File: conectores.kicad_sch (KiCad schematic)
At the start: 12 parts, among them J10 5v Input, J11 12v Input, J12 Temp DHT22, J2 Fan1 Conn, J3 Fan2 Conn, J4 Fan4 Conn, J5 Fan3 Conn, J6 Buzz Conn, J7 OLED, J8 Relay Ctrl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

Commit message: pop stashed changes
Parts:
- removed J10: 5v Input, Connector_PinHeader_2.54mm:PinHeader_1x02_P2.54mm_Vertical, symbol Connector:Conn_01x02_Male
- removed J11: 12v Input, Connector_PinHeader_2.54mm:PinHeader_1x02_P2.54mm_Vertical, symbol Connector:Conn_01x02_Male
- removed J6: Buzz Conn, Connector_PinHeader_2.54mm:PinHeader_1x03_P2.54mm_Vertical, symbol Connector:Conn_01x03_Male
- removed J8: Relay Ctrl, Connector_PinHeader_2.54mm:PinHeader_1x03_P2.54mm_Vertical, symbol Connector:Conn_01x03_Male
- removed J9: Relay Out, Connector_PinHeader_2.54mm:PinHeader_1x03_P2.54mm_Vertical, symbol Connector:Conn_01x03_Male
- removed JP1: NO/NC Selector, Connector_PinHeader_2.54mm:PinHeader_1x03_P2.54mm_Vertical, symbol Jumper:Jumper_3_Bridged12
- added C11, C2: 10uF, footprints descargados:CL21A106KOQNNNE, symbol CL21A106KOQNNNE:CL21A106KOQNNNE
- added C7: 10pF, Capacitor_SMD:C_0603_1608Metric_Pad1.08x0.95mm_HandSolder, symbol Device:C_Small
- added C8: 1uF, Capacitor_SMD:C_0603_1608Metric_Pad1.08x0.95mm_HandSolder, symbol Device:C_Small
- added D10: LED 12V, digikey-footprints:0805, symbol dk_LED-Indication-Discrete:LG_R971-KN-1
- added D4: LED 5V, digikey-footprints:0805, symbol dk_LED-Indication-Discrete:LG_R971-KN-1
- added D8: ES1D, Diode_SMD:D_1206_3216Metric_Pad1.42x1.75mm_HandSolder, symbol Device:D
- added F1: Polyfuse 0.5A, Fuse:Fuse_1206_3216Metric_Pad1.42x1.75mm_HandSolder, symbol Device:Polyfuse
- added J1: 12v Input, Connector_PinHeader_2.54mm:PinHeader_1x02_P2.54mm_Vertical, symbol Connector:Conn_01x02_Male
- added R16: 820k, Resistor_SMD:R_0603_1608Metric_Pad0.98x0.95mm_HandSolder, symbol Device:R
- added R21: 160k, Resistor_SMD:R_0603_1608Metric_Pad0.98x0.95mm_HandSolder, symbol Device:R
- added R22: 49.9k, Resistor_SMD:R_0603_1608Metric_Pad0.98x0.95mm_HandSolder, symbol Device:R
- added R8: 10k, Resistor_SMD:R_0603_1608Metric_Pad0.98x0.95mm_HandSolder, symbol Device:R
- added TP1: 5V, TestPoint:TestPoint_Pad_D1.5mm, symbol Connector:TestPoint
- added TP3: 12V, TestPoint:TestPoint_Pad_D1.5mm, symbol Connector:TestPoint
- added U2: TLV76701DGNR, footprints descargados:TLV76701DGNR, symbol TLV76701DGNR:TLV76701DGNR
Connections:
- net 12VFAN is gone; now on net 12V: J2.2 (Pin_2), J3.2 (Pin_2), J4.2 (Pin_2), J5.2 (Pin_2)
- net 12V: now also D8.2 (A), J1.2 (Pin_2), R22.1, TP3.1
- net 5V: now also F1.2, R8.1, TP1.1
- net GND: now also C11.2, C2.2, C8.2, D10.2, D4.2, J1.1 (Pin_1), R21.2, U2.4 (GND), U2.6 (GND), U2.EPAD; no longer J2.1 (Pin_1), J3.1 (Pin_1), J4.1 (Pin_1), J5.1 (Pin_1)
- new net: C2.1, C8.1, D8.1 (K), U2.5 (EN), U2.8 (IN)
- new net: C11.1, C7.1, F1.1, R16.1, U2.1 (OUT)
- new net: C7.2, R16.2, R21.1, U2.2 (FB)
- new net: D4.1, R8.2
- new net: D10.1, R22.2
- new net GNDFAN: J2.1 (Pin_1), J3.1 (Pin_1), J4.1 (Pin_1), J5.1 (Pin_1)
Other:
- note added: "10pF = 0.01nF"
- note added: "Deberian ser 840K para 5V"
- note added: "Power conversion 12v -> 5v"
- moved on the sheet: J12, J2, J3, J4, J5, J7

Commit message: minor text changes
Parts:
- J2: value Fan1 Conn -> Fan1
- J3: value Fan2 Conn -> Fan2
- J4: value Fan4 Conn -> Fan4
- J5: value Fan3 Conn -> Fan3
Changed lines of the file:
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@@
     (in_bom yes) (on_board yes)
     (property "Reference" "J2" (id 0) (at 68.58 97.155 0))
-    (property "Value" "Fan1 Conn" (id 1) (at 69.215 100.33 0))
+    (property "Value" "Fan1" (id 1) (at 69.215 100.33 0))
     (property "Footprint" "Connector:FanPinHeader_1x04_P2.54mm_Vertical" (id 2) (at 63.5 107.315 0)
       (effects (font (size 1.27 1.27)) hide)
@@
     (in_bom yes) (on_board yes)
     (property "Reference" "J5" (id 0) (at 91.44 97.79 0))
-    (property "Value" "Fan3 Conn" (id 1) (at 93.98 100.33 0))
+    (property "Value" "Fan3" (id 1) (at 93.98 100.33 0))
     (property "Footprint" "Connector:FanPinHeader_1x04_P2.54mm_Vertical" (id 2) (at 88.9 107.315 0)
       (effects (font (size 1.27 1.27)) hide)
@@
     (in_bom yes) (on_board yes)
     (property "Reference" "J3" (id 0) (at 67.945 116.84 0))
-    (property "Value" "Fan2 Conn" (id 1) (at 69.215 119.38 0))
+    (property "Value" "Fan2" (id 1) (at 69.215 119.38 0))
     (property "Footprint" "Connector:FanPinHeader_1x04_P2.54mm_Vertical" (id 2) (at 63.5 125.095 0)
       (effects (font (size 1.27 1.27)) hide)
@@
     (in_bom yes) (on_board yes)
     (property "Reference" "J4" (id 0) (at 91.44 116.84 0))
-    (property "Value" "Fan4 Conn" (id 1) (at 93.98 119.38 0))
+    (property "Value" "Fan4" (id 1) (at 93.98 119.38 0))
     (property "Footprint" "Connector:FanPinHeader_1x04_P2.54mm_Vertical" (id 2) (at 88.9 125.095 0)
       (effects (font (size 1.27 1.27)) hide)

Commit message: add drive high-side switch
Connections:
- net GNDFAN is gone; now on net GND: J2.1 (Pin_1), J3.1 (Pin_1), J4.1 (Pin_1), J5.1 (Pin_1)
- net 12V: no longer J2.2 (Pin_2), J3.2 (Pin_2), J4.2 (Pin_2), J5.2 (Pin_2)
- new net 12VF: J2.2 (Pin_2), J3.2 (Pin_2), J4.2 (Pin_2), J5.2 (Pin_2)
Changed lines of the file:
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@@
     (effects (font (size 1.27 1.27)) (justify left))
   )
-  (hierarchical_label "12V" (shape passive) (at 93.98 125.095 0)
+  (hierarchical_label "12VF" (shape passive) (at 93.98 125.095 0)
     (effects (font (size 1.27 1.27)) (justify left))
   )
-  (hierarchical_label "GNDFAN" (shape passive) (at 68.58 122.555 0)
+  (hierarchical_label "GND" (shape passive) (at 68.58 122.555 0)
     (effects (font (size 1.27 1.27)) (justify left))
   )
-  (hierarchical_label "12V" (shape passive) (at 93.98 107.315 0)
+  (hierarchical_label "12VF" (shape passive) (at 93.98 107.315 0)
     (effects (font (size 1.27 1.27)) (justify left))
   )
@@
     (effects (font (size 1.27 1.27)) (justify left))
   )
-  (hierarchical_label "12V" (shape passive) (at 68.58 125.095 0)
+  (hierarchical_label "12VF" (shape passive) (at 68.58 125.095 0)
     (effects (font (size 1.27 1.27)) (justify left))
   )
@@
     (effects (font (size 1.27 1.27)) (justify left))
   )
-  (hierarchical_label "GNDFAN" (shape passive) (at 68.58 104.775 0)
+  (hierarchical_label "GND" (shape passive) (at 68.58 104.775 0)
     (effects (font (size 1.27 1.27)) (justify left))
   )
-  (hierarchical_label "GNDFAN" (shape passive) (at 93.98 122.555 0)
+  (hierarchical_label "GND" (shape passive) (at 93.98 122.555 0)
     (effects (font (size 1.27 1.27)) (justify left))
   )
@@
     (effects (font (size 1.27 1.27)) (justify left))
   )
-  (hierarchical_label "12V" (shape passive) (at 68.58 107.315 0)
+  (hierarchical_label "12VF" (shape passive) (at 68.58 107.315 0)
     (effects (font (size 1.27 1.27)) (justify left))
   )
-  (hierarchical_label "GNDFAN" (shape passive) (at 93.98 104.775 0)
+  (hierarchical_label "GND" (shape passive) (at 93.98 104.775 0)
     (effects (font (size 1.27 1.27)) (justify left))
   )

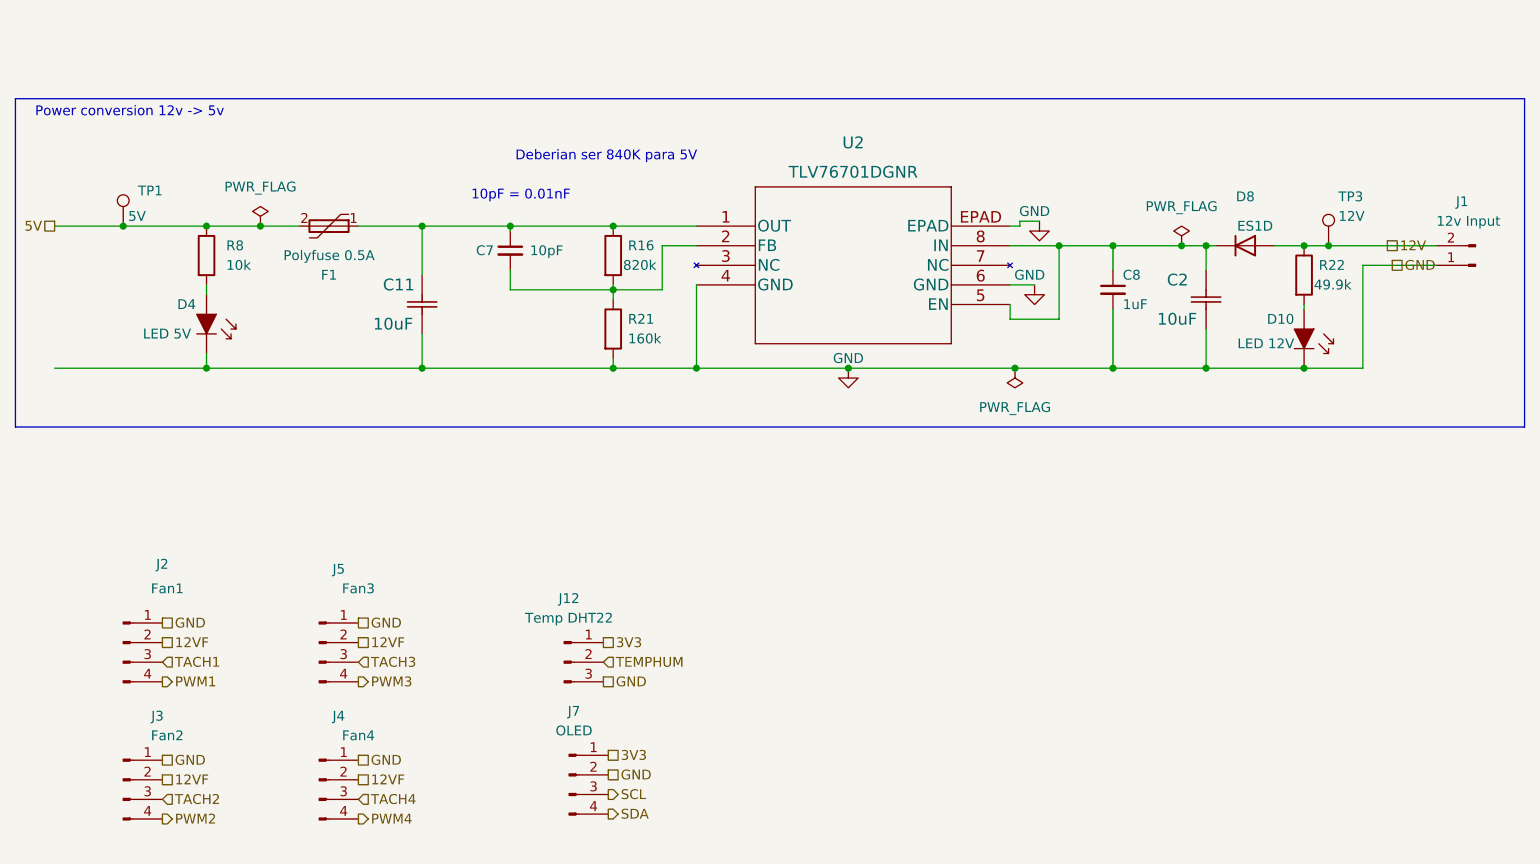
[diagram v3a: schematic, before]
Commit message: edit some footprints to give more room to the pads
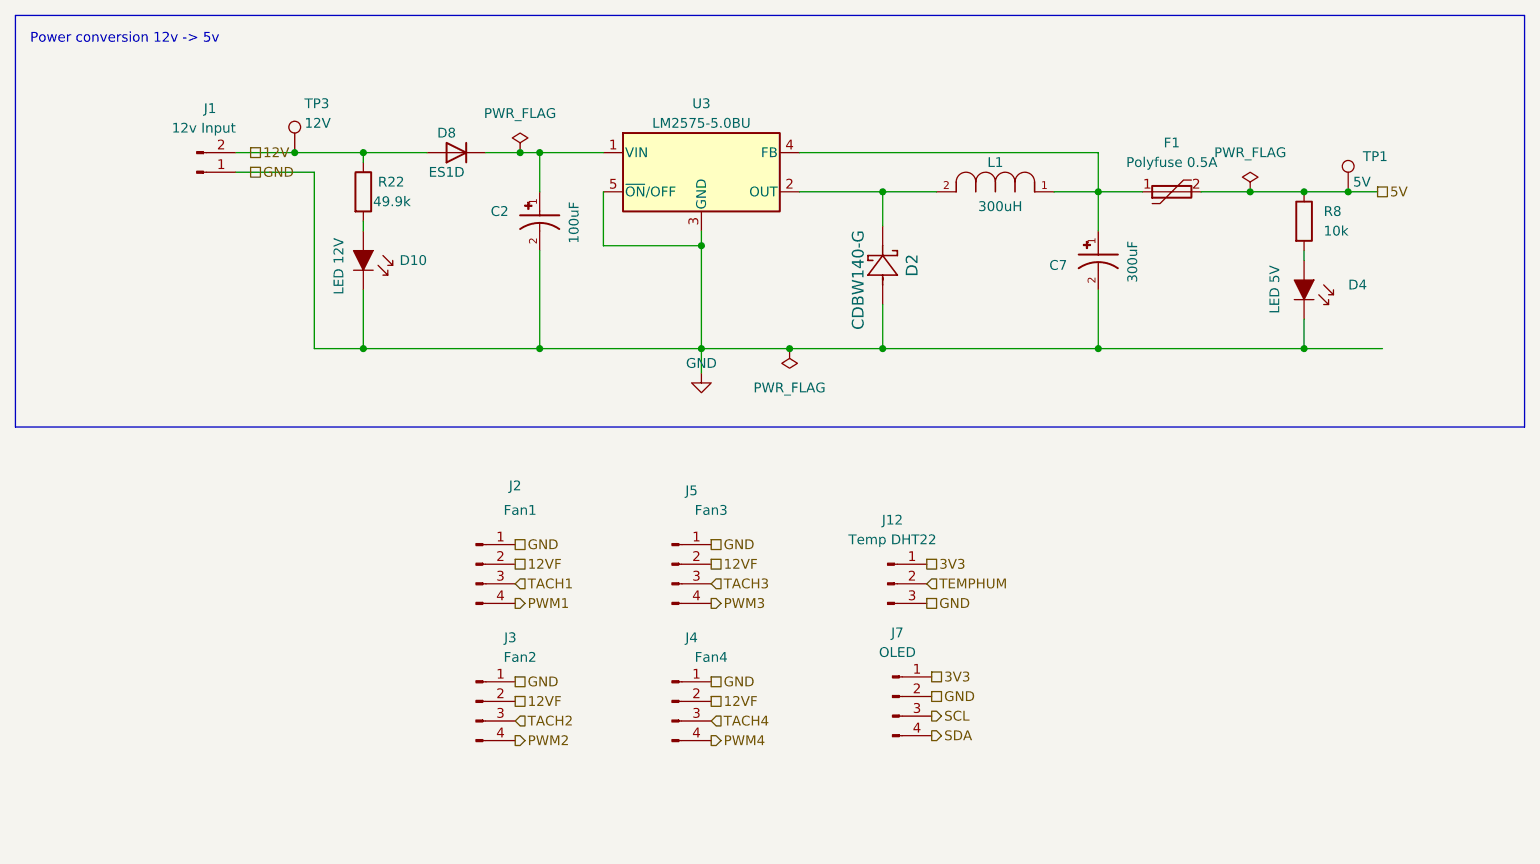
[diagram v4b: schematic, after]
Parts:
- removed C11, C2: 10uF, footprints descargados:CL21A106KOQNNNE, symbol CL21A106KOQNNNE:CL21A106KOQNNNE
- removed C7: 10pF, Capacitor_SMD:C_0603_1608Metric_Pad1.08x0.95mm_HandSolder, symbol Device:C_Small
- removed C8: 1uF, Capacitor_SMD:C_0603_1608Metric_Pad1.08x0.95mm_HandSolder, symbol Device:C_Small
- removed R16: 820k, Resistor_SMD:R_0603_1608Metric_Pad0.98x0.95mm_HandSolder, symbol Device:R
- removed R21: 160k, Resistor_SMD:R_0603_1608Metric_Pad0.98x0.95mm_HandSolder, symbol Device:R
- removed U2: TLV76701DGNR, footprints descargados:TLV76701DGNR, symbol TLV76701DGNR:TLV76701DGNR
- added C2: 100uF, footprints descargados:CAP_EEEHA1V101XP, symbol EEEHA1V101XP:EEEHA1V101XP
- added C7: 300uF, footprints descargados:CAP_EEEFT1V331AP, symbol EEEFT1V331AP:EEEFT1V331AP
- added D2: CDBW140-G, Diode_SMD:D_SOD-123F, symbol CDBW140-G:CDBW140-G
- added L1: 300uH, footprints descargados:DR127-331_INDM125125X800N, symbol DR127-331-R:DR127-331-R
- added U3: LM2575-5.0BU, Package_TO_SOT_SMD:TO-263-5_TabPin3, symbol Regulator_Switching:LM2575-5.0BU
- R22, R8: footprint Resistor_SMD:R_0603_1608Metric_Pad0.98x0.95mm_HandSolder -> Resistor_SMD:R_0805_2012Metric_Pad1.20x1.40mm_HandSolder
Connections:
- net GND: now also C2.2, C7.2, D2.2, U3.3 (GND), U3.5 (~{ON}/OFF)
- net at D8.1 (K): now also C2.1, U3.1 (VIN)
- net at F1.1: now also C7.1, L1.1, U3.4 (FB)
- new net: D2.1, L1.2, U3.2 (OUT)
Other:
- note removed: "10pF = 0.01nF"
- note removed: "Deberian ser 840K para 5V"
- moved on the sheet: D10, D4, D8, F1, J1, J12, J2, J3, J4, J5, J7, R22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

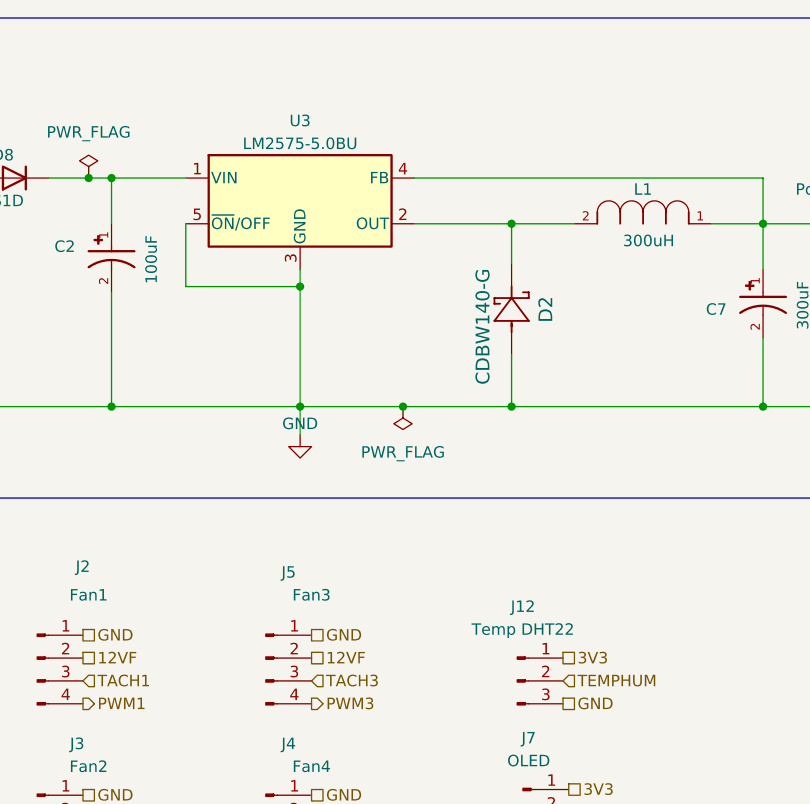
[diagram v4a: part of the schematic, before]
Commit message: synch sch and pcb
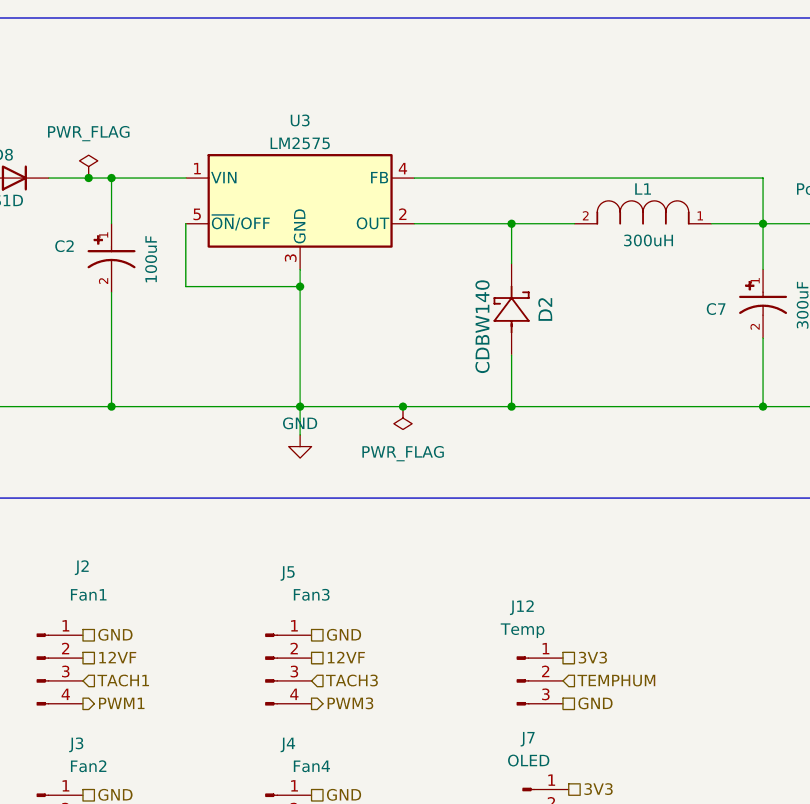
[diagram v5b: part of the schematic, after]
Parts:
- D2: value CDBW140-G -> CDBW140; Componente (none) -> CDBW140-G
- J1: footprint Connector_PinHeader_2.54mm:PinHeader_1x02_P2.54mm_Vertical -> Connector_PinHeader_2.54mm:PinHeader_1x02_P2.54mm_Horizontal
- J12: value Temp DHT22 -> Temp; footprint Connector_PinHeader_2.54mm:PinHeader_1x03_P2.54mm_Vertical -> Connector_PinHeader_2.54mm:PinHeader_1x03_P2.54mm_Horizontal
- J7: footprint Connector_PinHeader_2.54mm:PinHeader_1x04_P2.54mm_Vertical -> Connector_PinHeader_2.54mm:PinHeader_1x04_P2.54mm_Horizontal
- U3: value LM2575-5.0BU -> LM2575; Component (none) -> LM2575-5.0BU
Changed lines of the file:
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@@
     (in_bom yes) (on_board yes)
     (property "Reference" "U3" (id 0) (at 138.43 37.465 0))
-    (property "Value" "LM2575-5.0BU" (id 1) (at 138.43 40.005 0))
+    (property "Value" "LM2575" (id 1) (at 138.43 40.005 0))
     (property "Footprint" "Package_TO_SOT_SMD:TO-263-5_TabPin3" (id 2) (at 138.43 52.705 0)
       (effects (font (size 1.27 1.27) italic) (justify left) hide)
     )
     (property "Datasheet" "http://ww1.microchip.com/downloads/en/DeviceDoc/lm2575.pdf" (id 3) (at 138.43 46.355 0)
+      (effects (font (size 1.27 1.27)) hide)
+    )
+    (property "Component" "LM2575-5.0BU" (id 4) (at 138.43 46.355 0)
       (effects (font (size 1.27 1.27)) hide)
     )
@@
     (property "Reference" "J7" (id 0) (at 163.83 106.045 0))
     (property "Value" "OLED" (id 1) (at 163.83 108.585 0))
-    (property "Footprint" "Connector_PinHeader_2.54mm:PinHeader_1x04_P2.54mm_Vertical" (id 2) (at 163.195 114.3 0)
+    (property "Footprint" "Connector_PinHeader_2.54mm:PinHeader_1x04_P2.54mm_Horizontal" (id 2) (at 163.195 114.3 0)
       (effects (font (size 1.27 1.27)) hide)
     )
@@
       (effects (font (size 1.524 1.524)))
     )
-    (property "Value" "CDBW140-G" (id 1) (at 158.75 60.325 0)
+    (property "Value" "CDBW140" (id 1) (at 158.75 60.325 0)
       (effects (font (size 1.524 1.524)))
     )
@@
     (property "Datasheet" "" (id 3) (at 161.925 53.34 0)
       (effects (font (size 1.524 1.524)))
+    )
+    (property "Componente" "CDBW140-G" (id 4) (at 161.925 53.34 0)
+      (effects (font (size 1.27 1.27)) hide)
     )
     (pin "1")
@@
     (in_bom yes) (on_board yes) (fields_autoplaced)
     (property "Reference" "J12" (id 0) (at 163.195 91.44 0))
-    (property "Value" "Temp DHT22" (id 1) (at 163.195 93.98 0))
-    (property "Footprint" "Connector_PinHeader_2.54mm:PinHeader_1x03_P2.54mm_Vertical" (id 2) (at 162.56 99.695 0)
+    (property "Value" "Temp" (id 1) (at 163.195 93.98 0))
+    (property "Footprint" "Connector_PinHeader_2.54mm:PinHeader_1x03_P2.54mm_Horizontal" (id 2) (at 162.56 99.695 0)
       (effects (font (size 1.27 1.27)) hide)
     )
@@
       (effects (font (size 1.27 1.27)) (justify right))
     )
-    (property "Footprint" "Connector_PinHeader_2.54mm:PinHeader_1x02_P2.54mm_Vertical" (id 2) (at 73.025 46.355 0)
-      (effects (font (size 1.27 1.27)) hide)
-    )
+    (property "Footprint" "Connector_PinHeader_2.54mm:PinHeader_1x02_P2.54mm_Horizontal" (id 2) (at 73.025 46.355 0)
+      (effects (font (size 1.27 1.27)) hide)
+    )

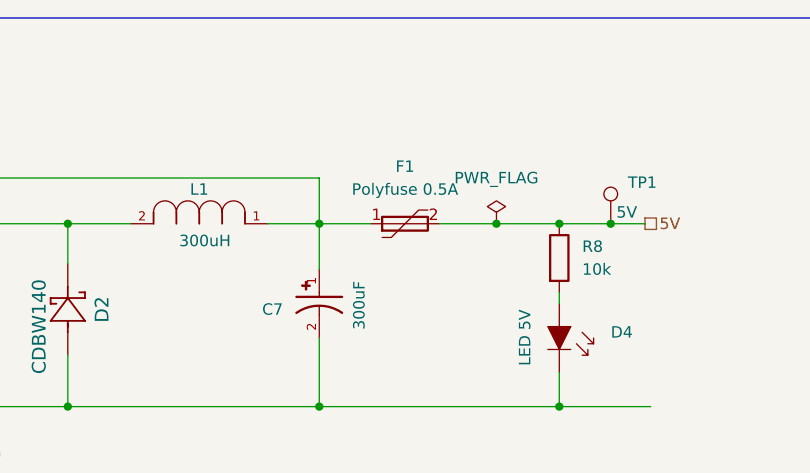
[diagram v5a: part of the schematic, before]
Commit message: Most SMD 1206 now
Also increase track size to 0.5 for Default subnet
And replace text so everything is more visible
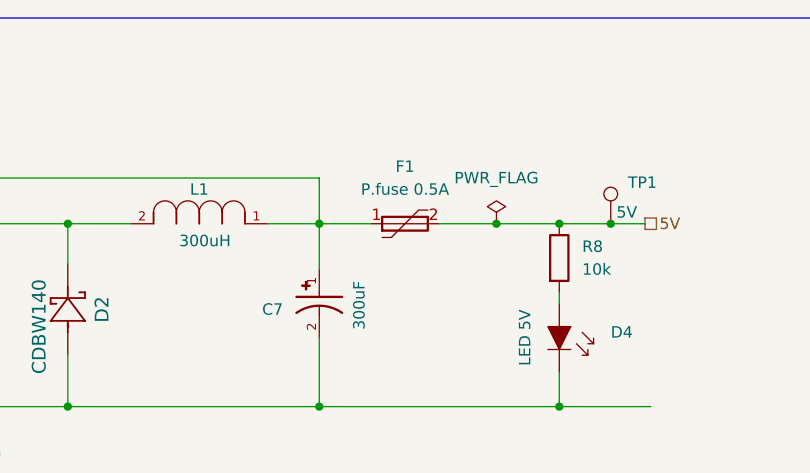
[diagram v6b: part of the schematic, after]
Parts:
- F1: value Polyfuse 0.5A -> P.fuse 0.5A
- R22, R8: footprint Resistor_SMD:R_0805_2012Metric_Pad1.20x1.40mm_HandSolder -> Resistor_SMD:R_1206_3216Metric_Pad1.30x1.75mm_HandSolder
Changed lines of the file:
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@@
       (effects (font (size 1.27 1.27)) (justify left))
     )
-    (property "Footprint" "Resistor_SMD:R_0805_2012Metric_Pad1.20x1.40mm_HandSolder" (id 2) (at 214.757 52.705 90)
+    (property "Footprint" "Resistor_SMD:R_1206_3216Metric_Pad1.30x1.75mm_HandSolder" (id 2) (at 214.757 52.705 90)
       (effects (font (size 1.27 1.27)) hide)
     )
@@
     (in_bom yes) (on_board yes)
     (property "Reference" "F1" (id 0) (at 199.39 42.545 90))
-    (property "Value" "Polyfuse 0.5A" (id 1) (at 199.39 45.085 90))
+    (property "Value" "P.fuse 0.5A" (id 1) (at 199.39 45.085 90))
     (property "Footprint" "Fuse:Fuse_1206_3216Metric_Pad1.42x1.75mm_HandSolder" (id 2) (at 204.47 47.625 0)
       (effects (font (size 1.27 1.27)) (justify left) hide)
@@
       (effects (font (size 1.27 1.27)) (justify left))
     )
-    (property "Footprint" "Resistor_SMD:R_0805_2012Metric_Pad1.20x1.40mm_HandSolder" (id 2) (at 92.837 48.895 90)
+    (property "Footprint" "Resistor_SMD:R_1206_3216Metric_Pad1.30x1.75mm_HandSolder" (id 2) (at 92.837 48.895 90)
       (effects (font (size 1.27 1.27)) hide)
     )
